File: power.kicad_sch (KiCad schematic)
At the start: 36 parts, among them IC1 TPS630702RNMR, J1 USB_C_Receptacle_USB2.0_16P, J8 1053141104, U5 L6983NQTR

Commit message: Names fix
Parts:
- C1, C2, C3: value 4.7u -> 4.7uf
- C18, C19, C22: value 22 uF -> 22uF
- L1: value 3.3u directional -> 3.3uh directional
- L2: value 1.5 uH -> 1.5uh
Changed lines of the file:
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@@
 			)
 		)
-		(property "Value" "22 uF"
+		(property "Value" "22uF"
 			(at 36.322 134.112 90)
 			(effects
@@
 			)
 		)
-		(property "Value" "4.7u"
+		(property "Value" "4.7uf"
 			(at 100.33 29.2162 0)
 			(effects
@@
 			)
 		)
-		(property "Value" "3.3u directional"
+		(property "Value" "3.3uh directional"
 			(at 48.26 38.0999 0)
 			(effects
@@
 			)
 		)
-		(property "Value" "22 uF"
+		(property "Value" "22uF"
 			(at 20.828 138.938 90)
 			(effects
@@
 			)
 		)
-		(property "Value" "4.7u"
+		(property "Value" "4.7uf"
 			(at 69.85 38.1062 0)
 			(effects
@@
 			)
 		)
-		(property "Value" "22 uF"
+		(property "Value" "22uF"
 			(at 36.322 127.762 90)
 			(effects
@@
 			)
 		)
-		(property "Value" "1.5 uH"
+		(property "Value" "1.5uh"
 			(at 106.68 105.918 0)
 			(effects
@@
 			)
 		)
-		(property "Value" "4.7u"
+		(property "Value" "4.7uf"
 			(at 27.94 38.1062 0)
 			(effects

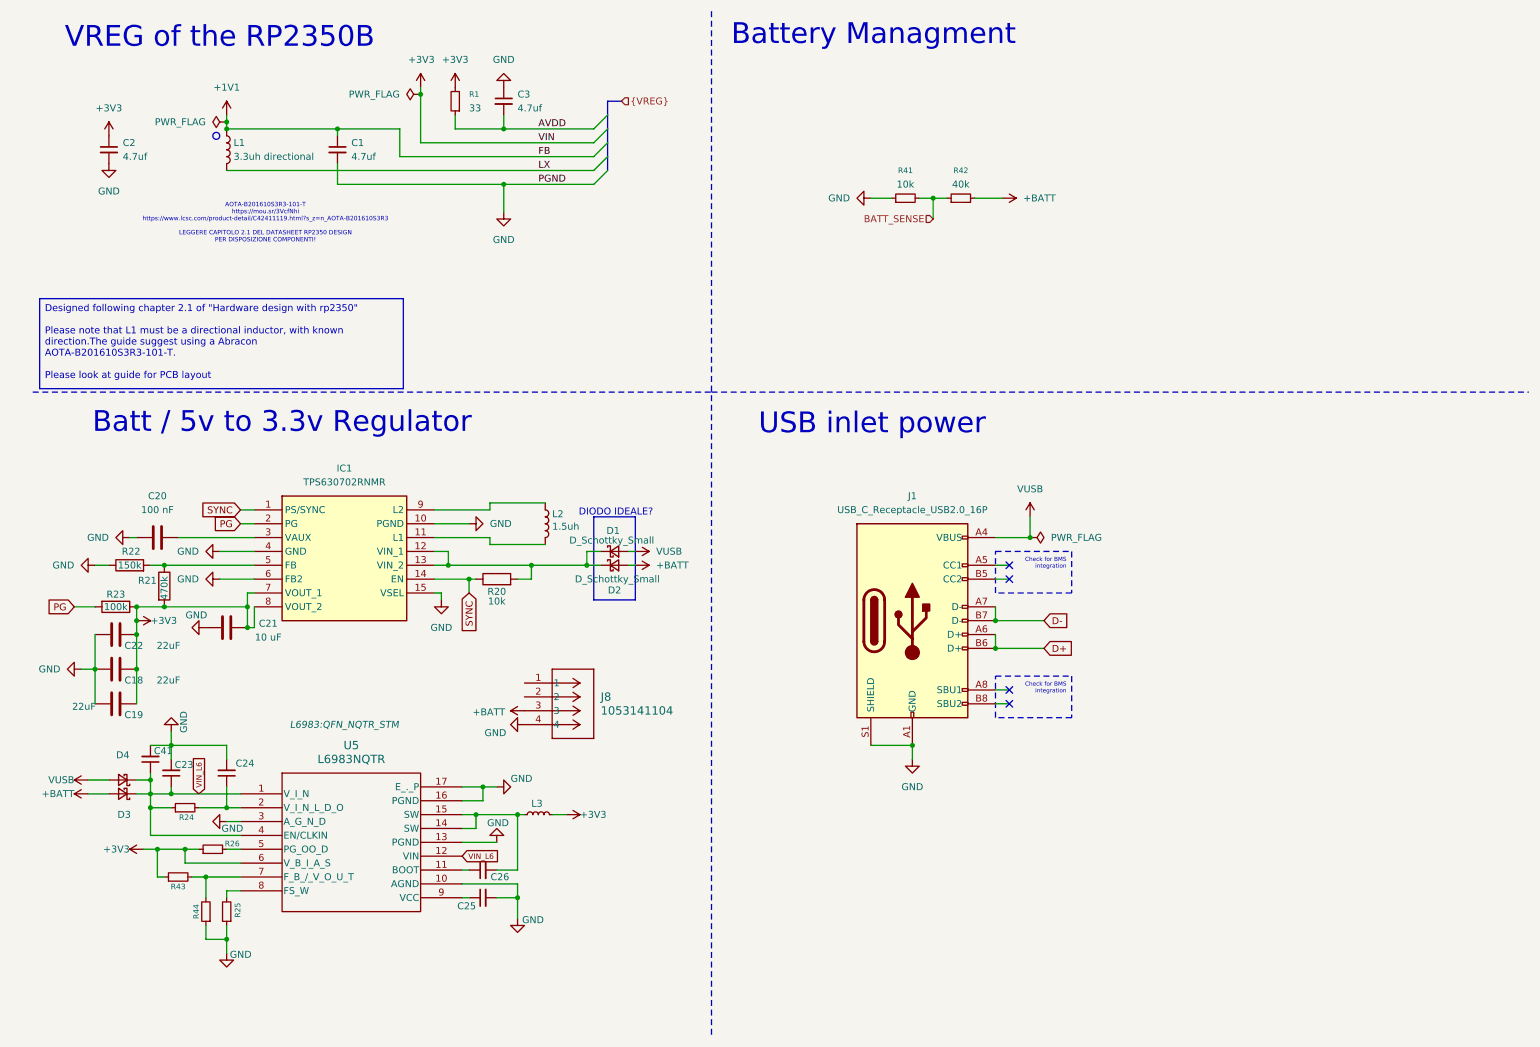
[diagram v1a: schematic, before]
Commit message: 10/01/2025
1v1 fix and v regulator final decision, general BOM corrections and allignments
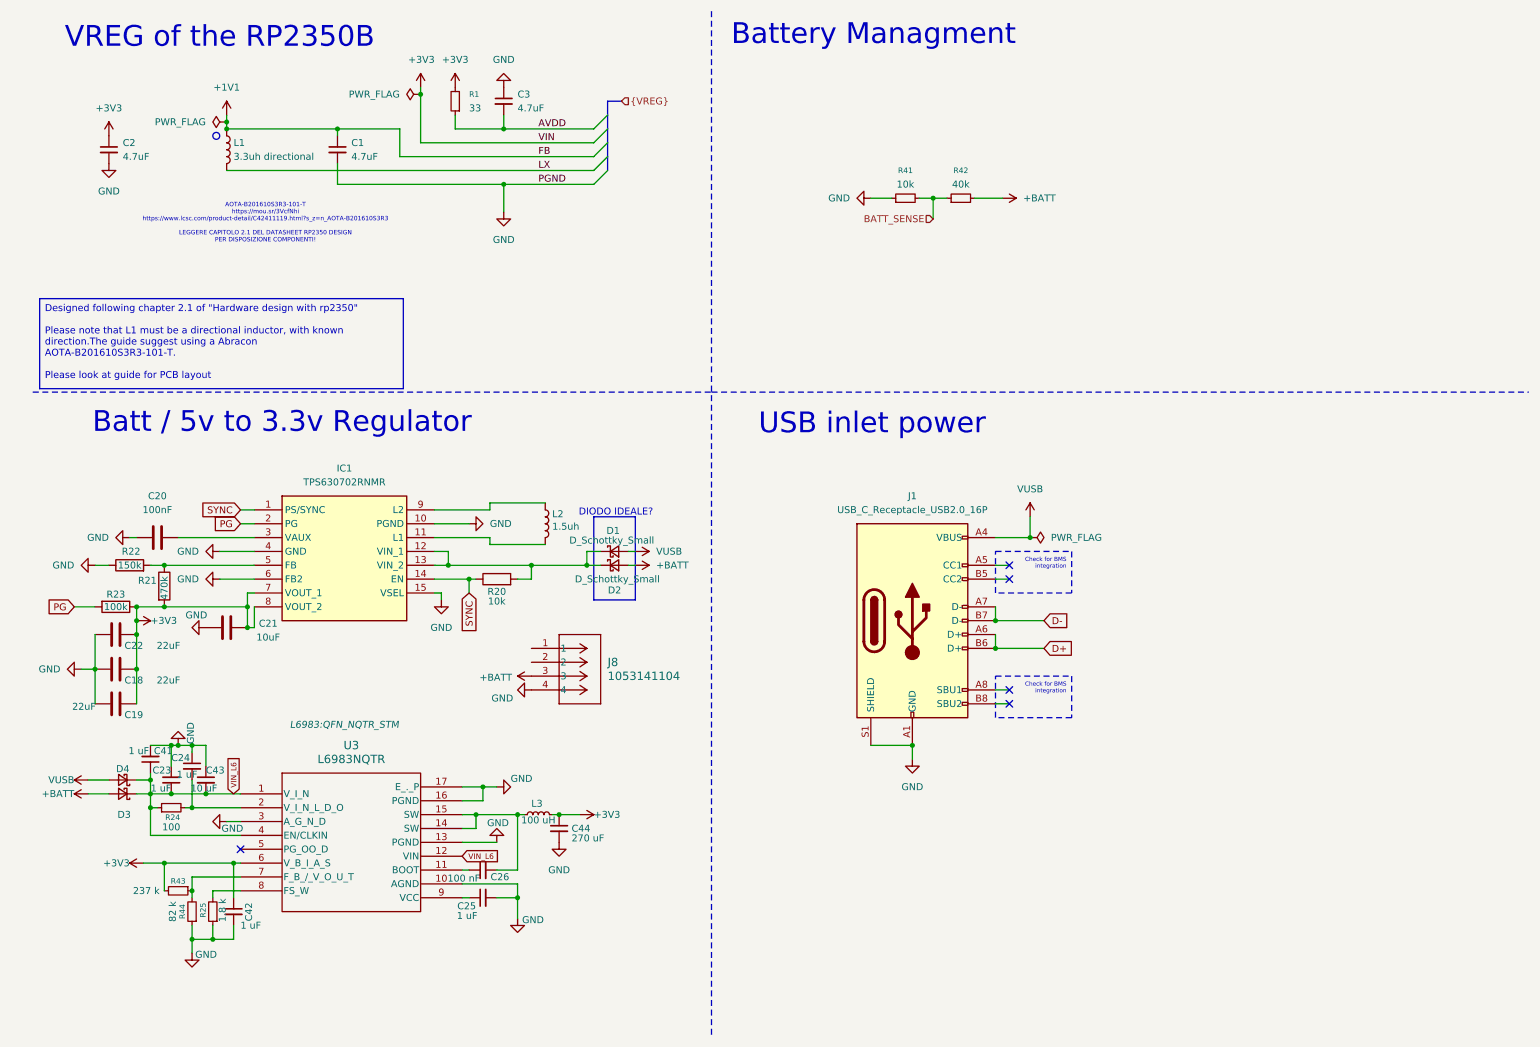
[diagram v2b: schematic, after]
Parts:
- removed R26: R_Small, Resistor_SMD:R_0603_1608Metric_Pad0.98x0.95mm_HandSolder, symbol Device:R_Small
- added C42: 1 uF, symbol Device:C_Small
- added C43: 10 uF, Capacitor_SMD:C_0603_1608Metric_Pad1.08x0.95mm_HandSolder, symbol Device:C_Small
- added C44: 270 uF, symbol Device:C_Small
- C1, C2, C3: value 4.7uf -> 4.7uF
- C20: value 100 nF -> 100nF
- C21: value 10 uF -> 10uF
- C23, C24, C25, C41: value C_Small -> 1 uF; now left out of the parts list
- C26: value C_Small -> 100 nF; now left out of the parts list
- D3, D4: now left out of the parts list
- J8: footprint CONN_SD-105314-100_04_MOL -> footprints:CONN_SD-105314-100_04_MOL
- L3: value L_Small -> 100 uH; now left out of the parts list
- R24: value R_Small -> 100; now left out of the parts list
- R25: value R_Small -> 1.8 k; now left out of the parts list
- R43: value R_Small -> 237 k; now left out of the parts list
- R44: value R_Small -> 82 k; now left out of the parts list
- U3: renamed from U5; now left out of the parts list
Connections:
- net +3V3: now also R43.2, C42.1, C44.1; no longer R43.1
- net GND: now also C24.1, C42.2, C43.1, C44.2; no longer C24.2
- net VIN_L6: now also C43.2
- net at R24.2, U3.2 (V_I_N_L_D_O): now also C24.2; no longer C24.1
- net at R44.2, U3.7 (F_B_/_V_O_U_T): now also R43.1; no longer R43.2
- no-connect marks 4 -> 5
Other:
- moved on the sheet: C23, C24, J8, R24, R25, R43, R44

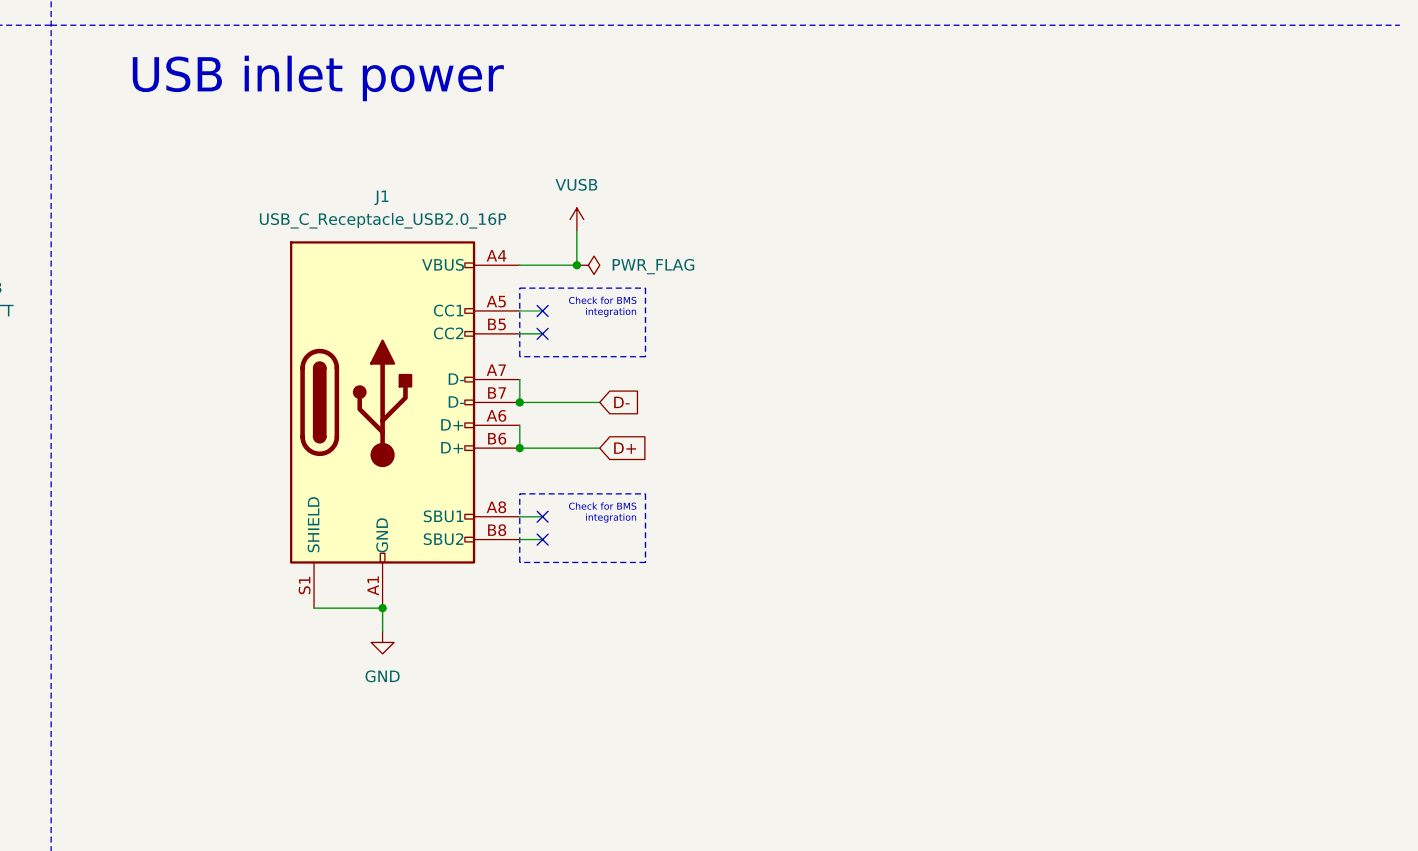
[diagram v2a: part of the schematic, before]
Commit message: Changed USB (before first order)
changed USB footprint to new one.
Added the CC pull-downs to garantee power delivery.
Other small details.
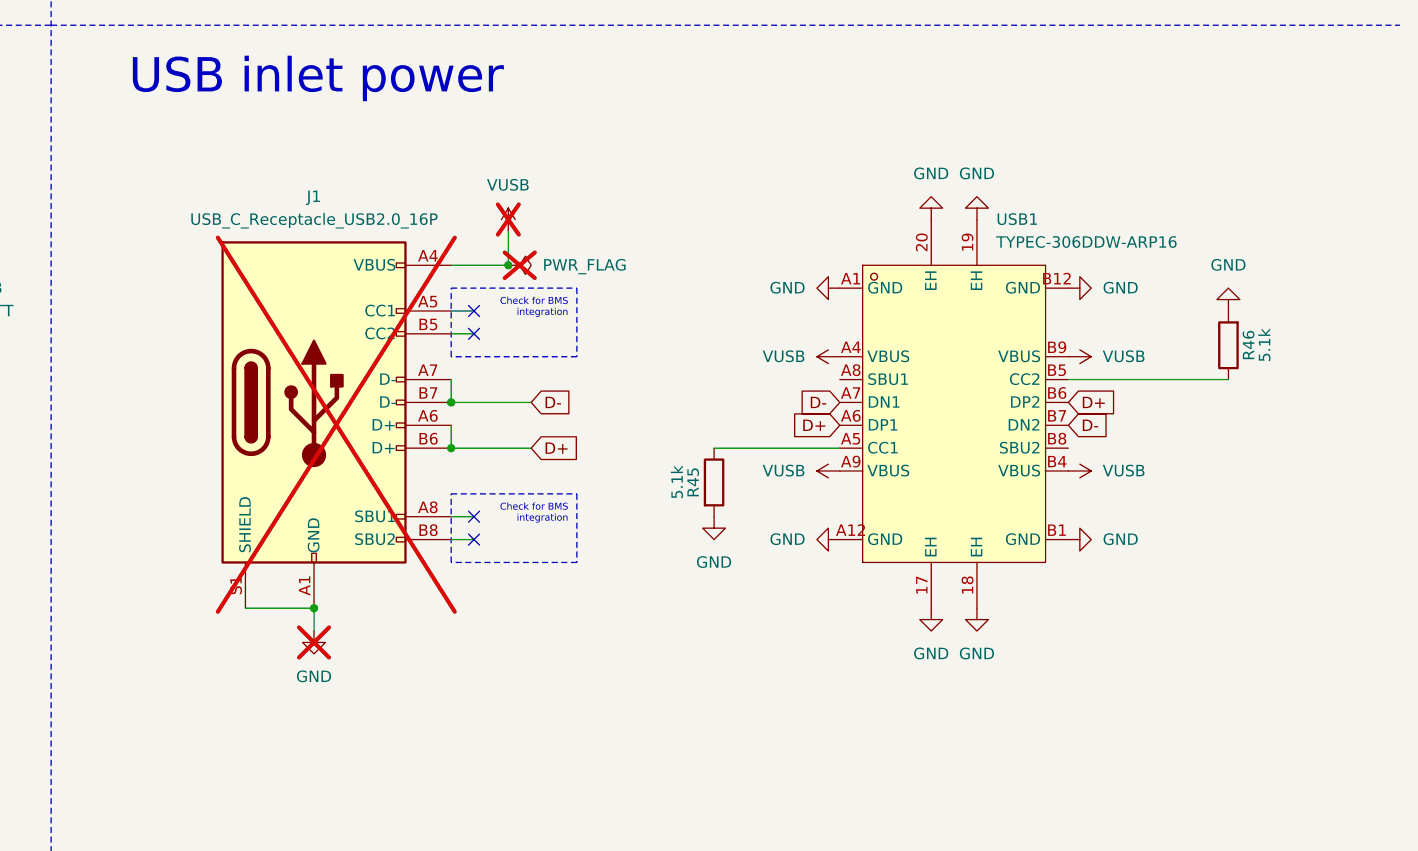
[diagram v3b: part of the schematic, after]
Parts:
- added R45, R46: 5.1k, Resistor_SMD:R_0603_1608Metric_Pad0.98x0.95mm_HandSolder, symbol Device:R
- added USB1: TYPEC-306DDW-ARP16, usb_c:USB-C-TH_TYPEC-306DDW-ARP16, symbol TYPEC-306DDW-ARP16:TYPEC-306DDW-ARP16
- J1: now not fitted; now left out of the parts list
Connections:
- net D+: now also USB1.A6 (DP1), USB1.B6 (DP2)
- net D-: now also USB1.A7 (DN1), USB1.B7 (DN2)
- net GND: now also R45.2, R46.2, USB1.17 (EH), USB1.18 (EH), USB1.19 (EH), USB1.20 (EH), USB1.A1 (GND), USB1.A12 (GND), USB1.B1 (GND), USB1.B12 (GND)
- net VUSB: now also USB1.A4 (VBUS), USB1.A9 (VBUS), USB1.B4 (VBUS), USB1.B9 (VBUS)
- new net: R45.1, USB1.A5 (CC1)
- new net: R46.1, USB1.B5 (CC2)
